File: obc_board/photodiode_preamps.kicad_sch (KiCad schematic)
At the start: 30 parts

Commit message: updated footprints
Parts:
- C? (x6): footprint (none) -> Capacitor_SMD:C_0402_1005Metric; Digikey Part Number (none) -> 490-GJM1555C1H160FB01JCT-ND
- D_IN? (x6): footprint (none) -> Connector_Molex:Molex_PicoBlade_53261-0271_1x02-1MP_P1.25mm_Horizontal; Digikey Part Number (none) -> WM25389CT-ND
- R? (x6): footprint (none) -> Resistor_SMD:R_0402_1005Metric; Digikey Part Number (none) -> YAG2303CT-ND
- U? (x9): footprint (none) -> Package_SO:MSOP-8_3x3mm_P0.65mm

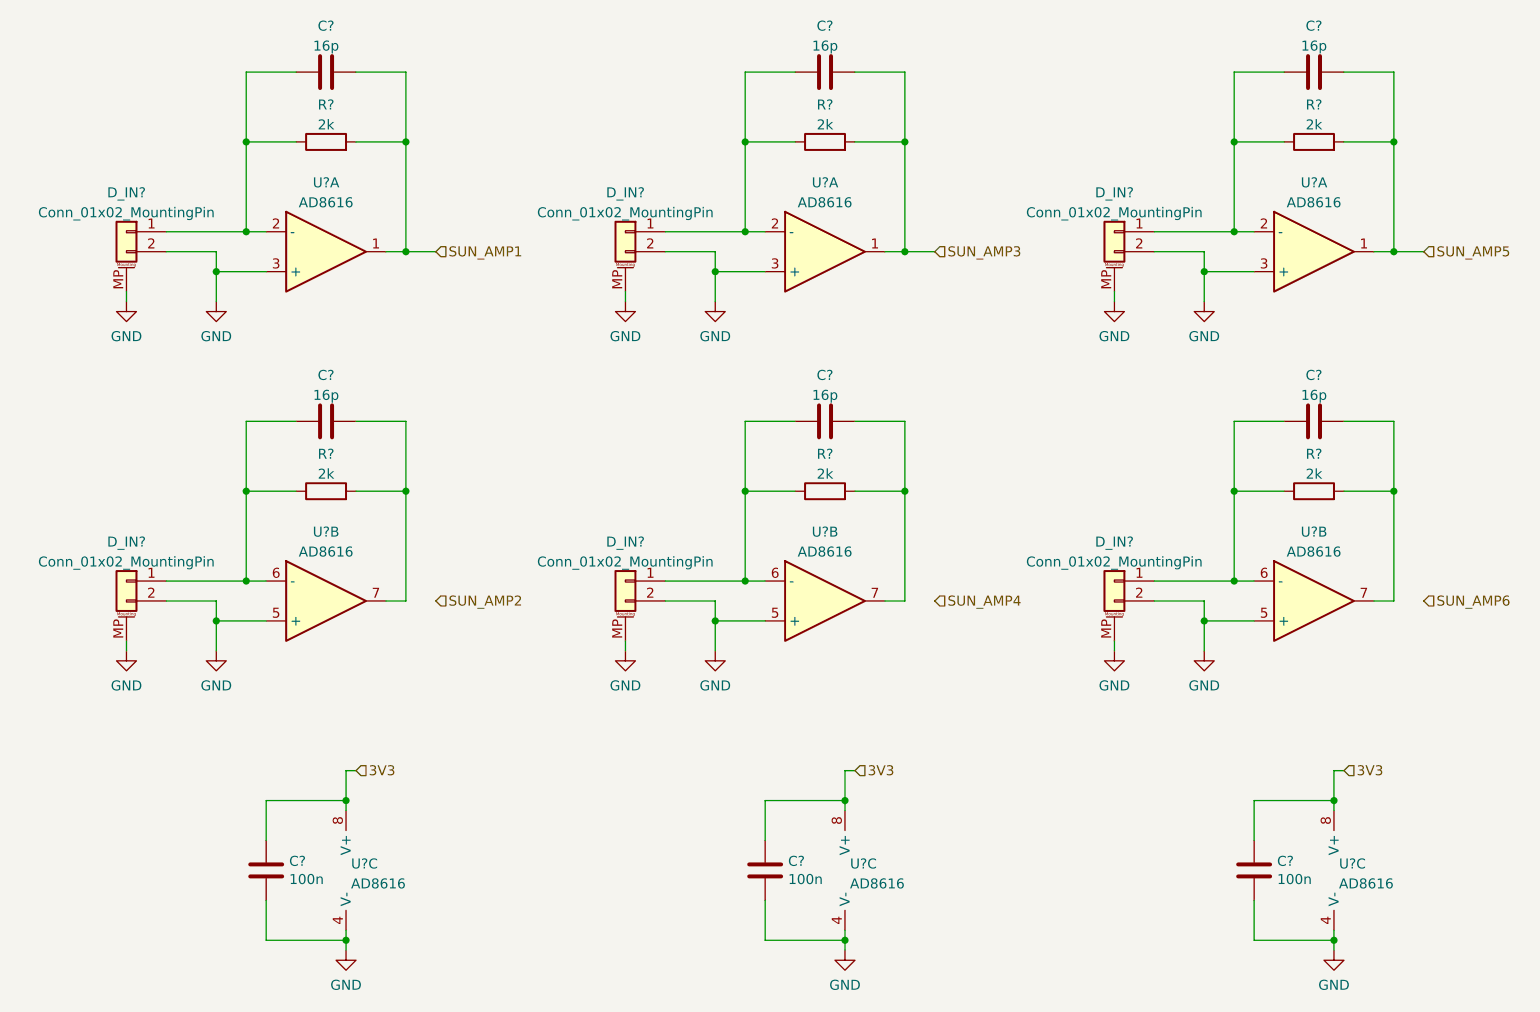
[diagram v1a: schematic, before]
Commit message: remapped magnetorquer pins, routed tespoints
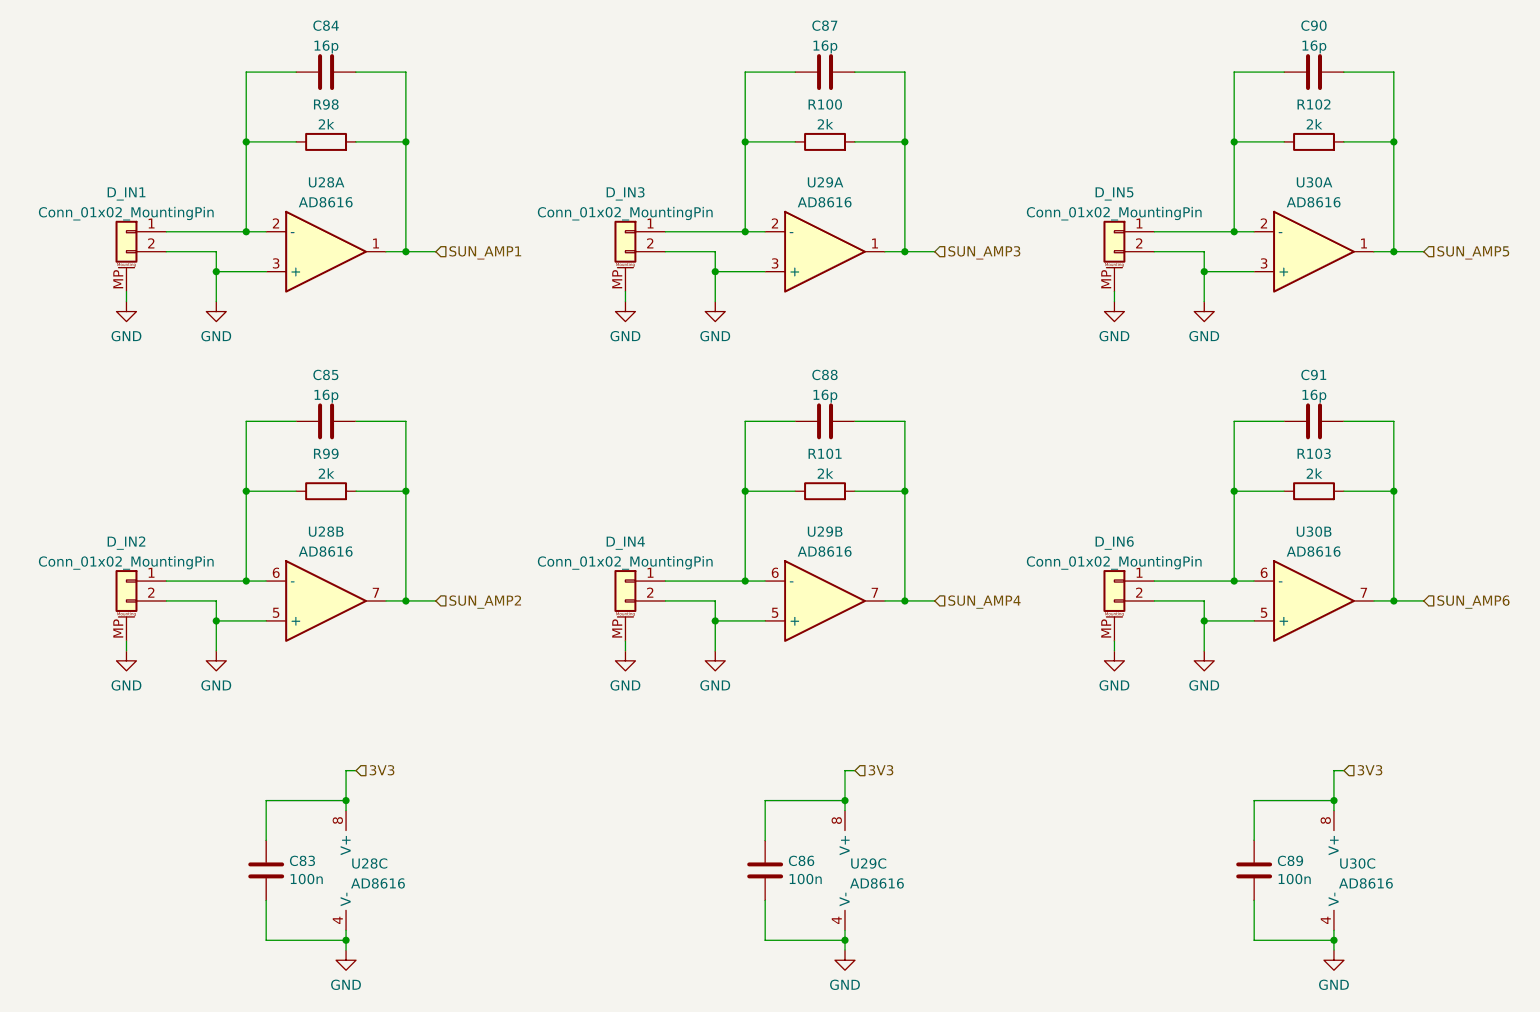
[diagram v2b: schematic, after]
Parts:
- gave numbers to parts that had none: 24
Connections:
- net SUN_AMP2: now also C85.2, R99.2, U28.7
- net SUN_AMP4: now also C88.2, R101.2, U29.7
- net SUN_AMP6: now also C91.2, R103.2, U30.7
